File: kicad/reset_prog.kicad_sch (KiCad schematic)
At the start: 13 parts, among them Q1 RE1C002UNTCL, SW1 CUS-12TB, SW2 EVQ-P7B01P, U2 TS3A4751RUCR

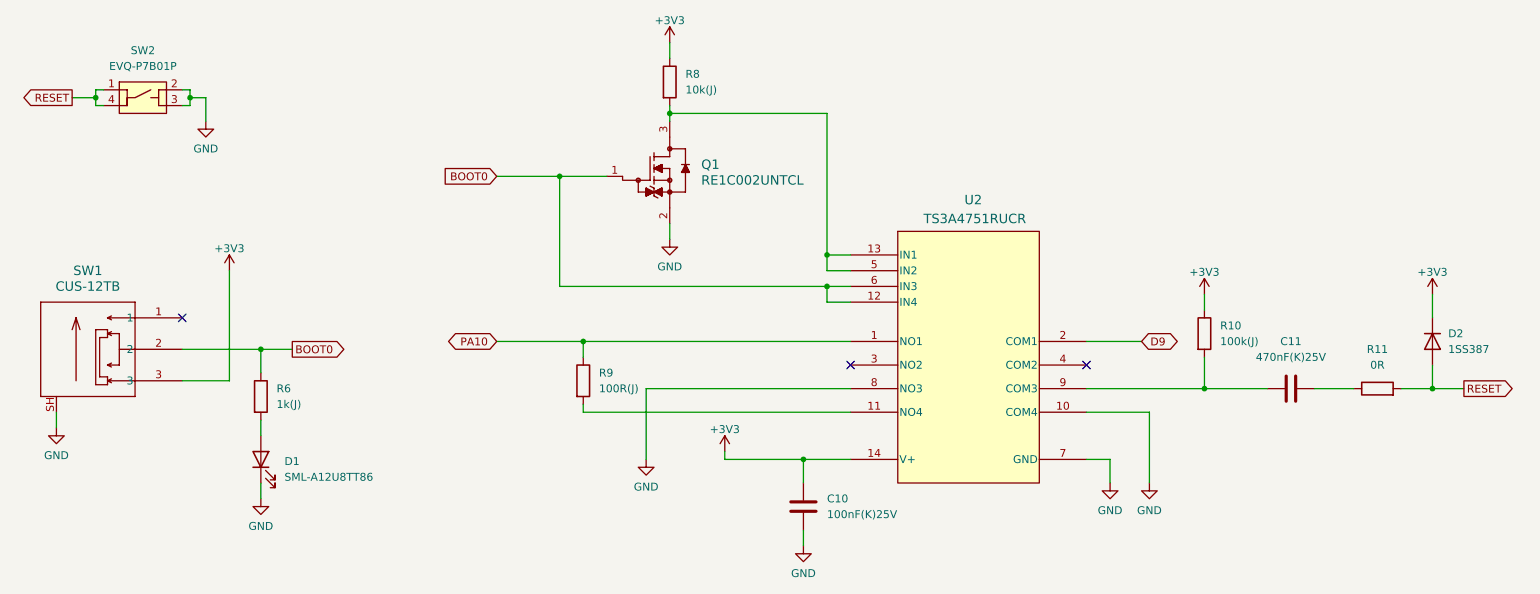
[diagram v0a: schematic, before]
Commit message: BOMを追加
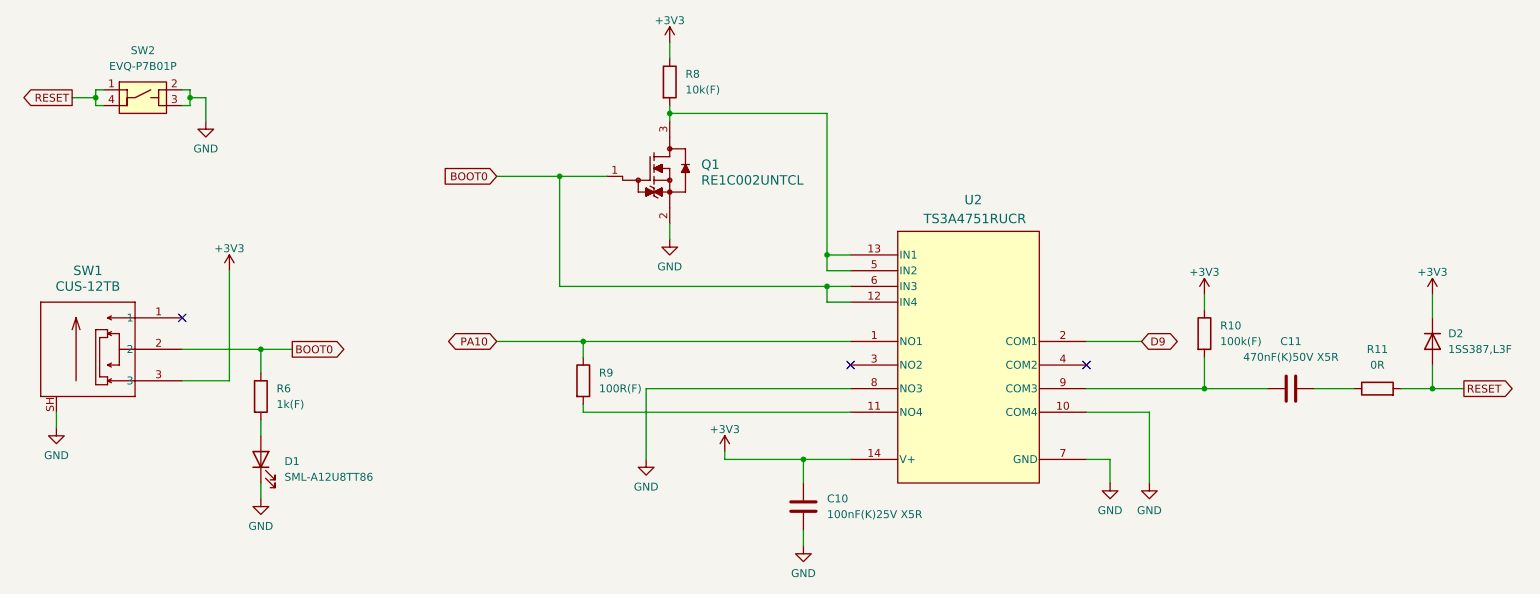
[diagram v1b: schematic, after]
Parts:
- C10: value 100nF(K)25V -> 100nF(K)25V X5R; MANUFACTURER (none) -> Murata Electronics; MPN (none) -> GRM033R61E104KE14D
- C11: value 470nF(K)25V -> 470nF(K)50V X5R; MANUFACTURER (none) -> Murata Electronics; MPN (none) -> GRM155R61H474KE11D
- D1: MANUFACTURER (none) -> Rohm Semiconductor; MPN (none) -> SML-A12U8TT86
- D2: value 1SS387 -> 1SS387,L3F; MANUFACTURER (none) -> Toshiba Semiconductor and Storage; MPN (none) -> 1SS387,L3F
- Q1: MANUFACTURER (none) -> Rohm Semiconductor; MPN (none) -> RE1C002UNTCL
- R10: value 100k(J) -> 100k(F); MANUFACTURER (none) -> YAGEO; MPN (none) -> RC0402FR-07100KL
- R11: MANUFACTURER (none) -> YAGEO; MPN (none) -> RC0402JR-070RL
- R6: value 1k(J) -> 1k(F); MANUFACTURER (none) -> YAGEO; MPN (none) -> RC0402FR-071KL
- R8: value 10k(J) -> 10k(F); MANUFACTURER (none) -> YAGEO; MPN (none) -> RC0402FR-0710KL
- R9: value 100R(J) -> 100R(F); MANUFACTURER (none) -> YAGEO; MPN (none) -> RC0402FR-07100RL
- SW1: MANUFACTURER (none) -> Nidec Components Corporation; MPN (none) -> CUS-12TB
- SW2: MANUFACTURER (none) -> Panasonic Electronic Components; MPN (none) -> EVQ-P7B01P
- U2: MANUFACTURER (none) -> Texas Instruments; MPN (none) -> TS3A4751RUCR
